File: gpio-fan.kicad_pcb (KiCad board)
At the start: 2 copper layers, 36 x 30.8 mm, 38 parts, among them J1 Conn_01x05, J10 Conn_01x04 DNS, J2 Conn_01x05 DNS, J3 Conn_01x02, J4 Conn_02x07_Odd_Even, J5 Conn_01x04 DNS, J6 Conn_01x02, J7 Conn_01x02 DNS, J8 Conn_01x02 DNS, J9 Conn_01x04 DNS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

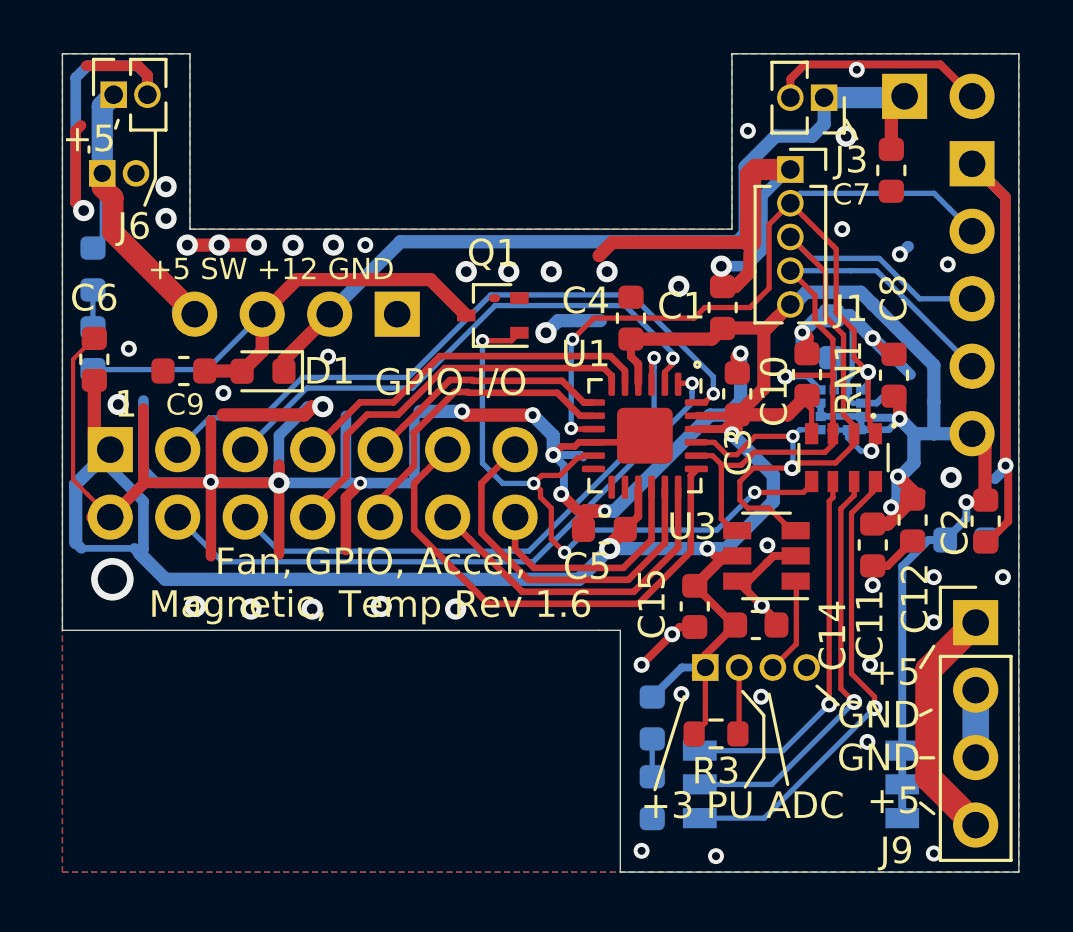
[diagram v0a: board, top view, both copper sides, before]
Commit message: Made minimum via hole size 0.3mm.  Bump to 1.7 due to layout changes.
Signed-off-by: Aaron Williams <aaron.w2@gmail.com>
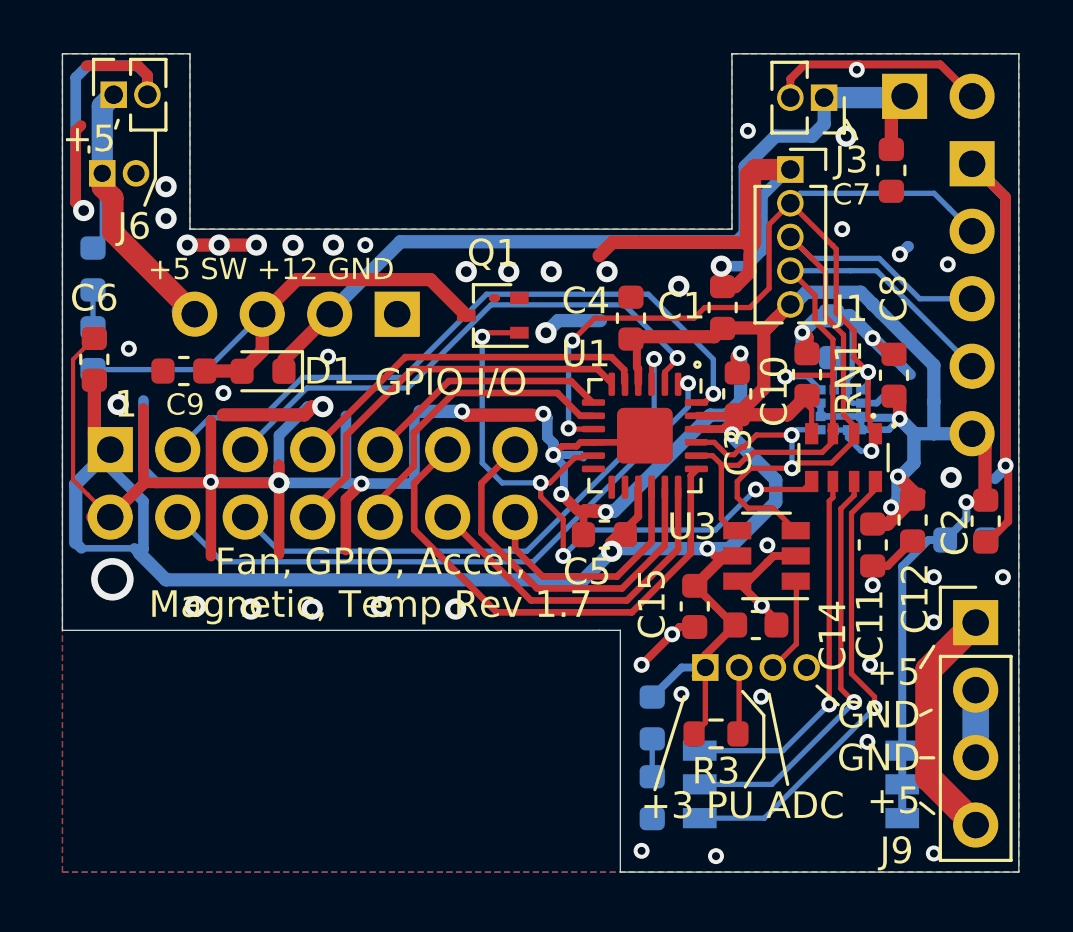
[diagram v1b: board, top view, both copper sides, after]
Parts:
- moved C5 0.20 mm to (70.4, 60.1)
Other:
- rule via_min_drill: 0.254 -> 0.3
- rule via_min_size: 0.508 -> 0.6
- board text added: "Fan, GPIO, Accel, Magnetic, Temp Rev 1.7"
- board text removed: "Fan, GPIO, Accel, Magnetic, Temp Rev 1.6"

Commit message: Changed accelerometer due to unavailability
The LSM303AGRTR compass/accelerometer/etc. is out of stock in many places
so this substitutes a LSM6DSL and a LISMDLTR combination instead.

Signed-off-by: Aaron Williams <aaron.w2@gmail.com>
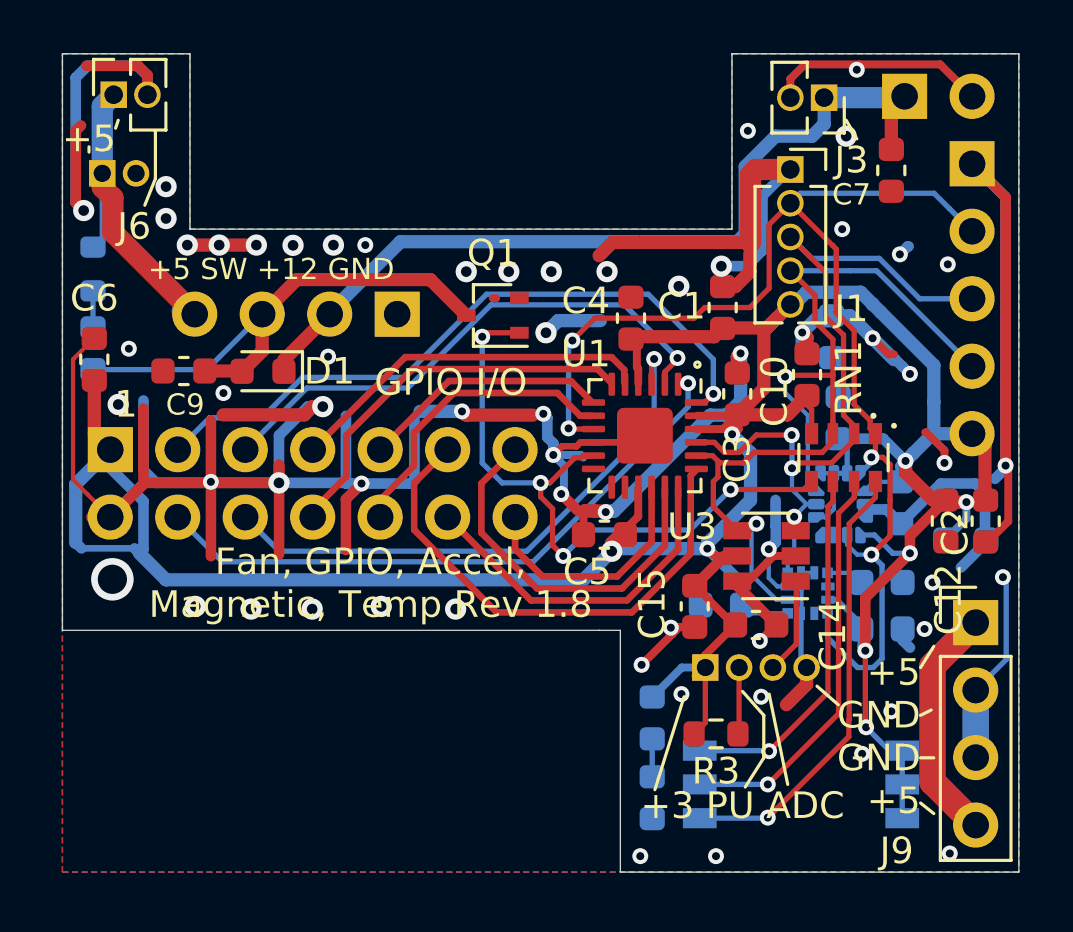
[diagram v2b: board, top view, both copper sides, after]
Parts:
- added C10: 0.1uF, Capacitor_SMD:C_0603_1608Metric, B.Cu at (74.8, 62.8)
- added C16: 0.1uF, Capacitor_SMD:C_0603_1608Metric, B.Cu at (80.8, 63.6)
- added C17: 0.1uF, Capacitor_SMD:C_0603_1608Metric, B.Cu at (80.8, 61.9)
- added U4: LIS3MDLTR, digikey-footprints:VFLGA-12_2x2mm, B.Cu at (78.0, 62.3)
- C11, C8: moved to B.Cu
- R1: value 1K -> 4.7K
- R2: value 100 -> 3.9K
- U2: value LSM303AGRTR -> LSM6DSL; footprint Package_LGA:LGA-12_2x2mm_P0.5mm -> Package_LGA:LGA-14_3x2.5mm_P0.5mm_LayoutBorder3x4y
- moved U2 3.55 mm to (79.3, 59.0), turned to 270 degrees
- moved C8 2.64 mm to (79.2, 55.7)
- moved C11 1.90 mm to (81.5, 58.9)
- moved C12 1.25 mm to (83.2, 59.6)
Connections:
- U2 pad 1: /SCL -> +3V3
- U2 pad 10: +3V3 -> Net-(U2-Pad10)
- U2 pad 11: /~INT -> Net-(U2-Pad11)
- U2 pad 12: /~INT -> +3V3
- U2 pad 4: /SDA -> /~INT
- U2 pad 5: Net-(C10-Pad1) -> +3V3
- U2 pad 7: /~INT -> GND
- U2 pad 8: GND -> +3V3
- U2 pad 9: +3V3 -> /~INT
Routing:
- net GND: track 182.2 -> 203.9 mm
- net /~INT: track 37.1 -> 48.9 mm
- net +3V3: track 124.0 -> 134.4 mm, vias 7 -> 8
- net /SDA: track 27.4 -> 35.4 mm, vias 1 -> 2
- net /SCL: track 31.3 -> 29.8 mm, vias 2 -> 3
- net Net-(C17-Pad1): track 0.00 -> 1.43 mm
- net Net-(C10-Pad1): track 1.24 -> 0.14 mm
- net /~INT_PU: track 17.6 -> 16.9 mm
- net /SDA_PU: track 15.8 -> 15.3 mm
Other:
- board text added: "Fan, GPIO, Accel, Magnetic, Temp Rev 1.8"
- board text removed: "+3 PU ADC GND"
- board text removed: "Fan, GPIO, Accel, Magnetic, Temp Rev 1.7"
- board text removed: "I2C TERM"

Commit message: Changed sensor to LSM9DS1TR due to availability issues.
Signed-off-by: Aaron Williams <aaron.w2@gmail.com>
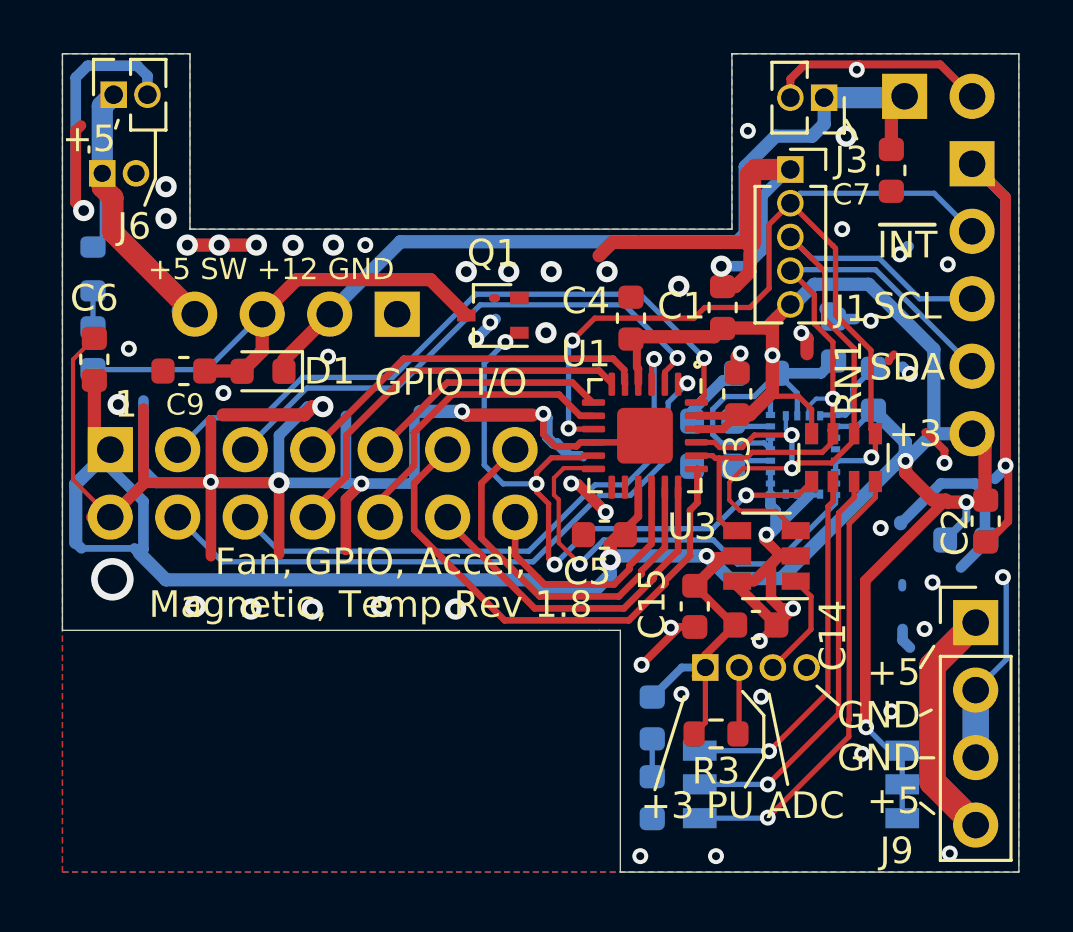
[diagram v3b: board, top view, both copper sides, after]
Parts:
- removed the C10 at (74.8, 62.8)
- removed the C10 at (78.0, 54.1)
- removed the C10 at (79.0, 52.6)
- removed C17: 0.1uF, Capacitor_SMD:C_0603_1608Metric
- removed U4: LIS3MDLTR, digikey-footprints:VFLGA-12_2x2mm
- added C10: 0.01uF, Capacitor_SMD:C_0603_1608Metric, B.Cu at (74.5, 57.5)
- C12: moved to B.Cu
- U2: value LSM6DSL -> LSM9DS1; footprint Package_LGA:LGA-14_3x2.5mm_P0.5mm_LayoutBorder3x4y -> Package_LGA:LGA-24L_3x3.5mm_P0.43mm
- moved C16 10.1 mm to (74.5, 55.8), turned to 180 degrees
- moved C12 8.02 mm to (79.0, 52.8), turned to 90 degrees
- moved C11 7.29 mm to (76.1, 54.0), turned to 180 degrees
- moved U2 2.33 mm to (77.9, 57.1)
- moved C8 1.71 mm to (80.5, 54.6)
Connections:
- C16 pad 1: +3V3 -> Net-(C16-Pad1)
- U2 pad 10: Net-(U2-Pad10) -> /~INT
- U2 pad 11: Net-(U2-Pad11) -> /~INT
- U2 pad 12: +3V3 -> /~INT
- U2 pad 13: /SCL -> Net-(U1-Pad12)
- U2 pad 14: /SDA -> GND
- U2 pad 2: +3V3 -> /SCL
- U2 pad 4: /~INT -> /SDA
- U2 pad 5: +3V3 -> GND
- U2 pad 7: GND -> +3V3
- U2 pad 9: /~INT -> Net-(U2-Pad9)
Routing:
- net GND: track 203.9 -> 186.8 mm, vias 61 -> 64
- net Net-(U1-Pad12): track 0.00 -> 16.9 mm, vias 0 -> 1
- net /~INT: track 48.9 -> 36.8 mm, vias 4 -> 3
- net /SDA: track 35.4 -> 25.9 mm, vias 2 -> 1
- net /SCL: track 29.8 -> 31.3 mm, vias 3 -> 2
- net Net-(C16-Pad1): track 0.00 -> 1.48 mm
- net Net-(C17-Pad1): track 1.43 -> 0.00 mm
- net Net-(C10-Pad1): track 0.14 -> 1.49 mm
- net +3V3: track 134.4 -> 135.4 mm, vias 8 -> 6
- net /P0_3: track 21.3 -> 22.0 mm
- net /P0_1: track 23.6 -> 24.2 mm
- net /P0_0: track 25.6 -> 25.0 mm
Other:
- board text added: "+3"
- board text added: "3.3V"
- board text added: "GND"
- board text added: "SCL"
- board text added: "SDA"
- board text added: "~INT"
- board text removed: "GND ~INT~ SCL SDA 3"
